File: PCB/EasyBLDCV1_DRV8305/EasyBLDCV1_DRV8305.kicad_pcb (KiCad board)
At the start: 4 copper layers, 71 parts, among them J1 10159560-A00221RLF, J2 TC2050-IDC, Q1 CSD16556Q5B, Q2 CSD16556Q5B, Q3 CSD16556Q5B, Q4 CSD16556Q5B, Q5 CSD16556Q5B, Q6 CSD16556Q5B, U1 DRV83053PHP, U2 TMS320F28027FPTT, U3 TPD4E05U06DQAR, U4 LMR16006XDDCR

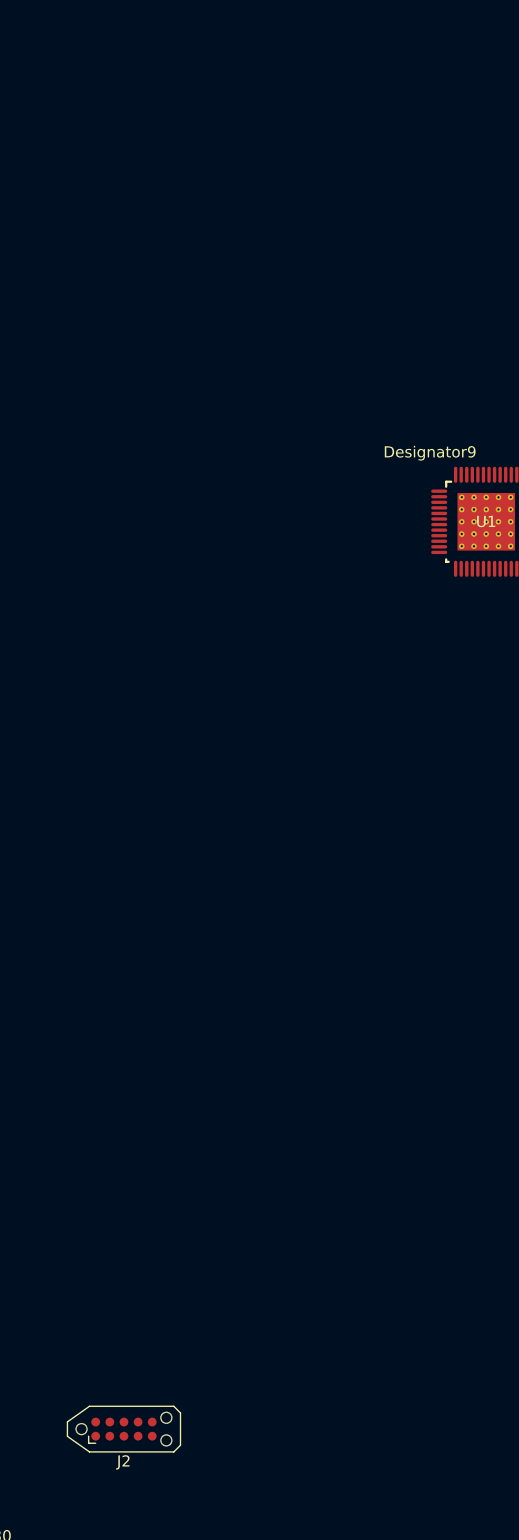
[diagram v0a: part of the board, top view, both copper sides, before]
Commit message: Updated Schematic With Missing Footprints
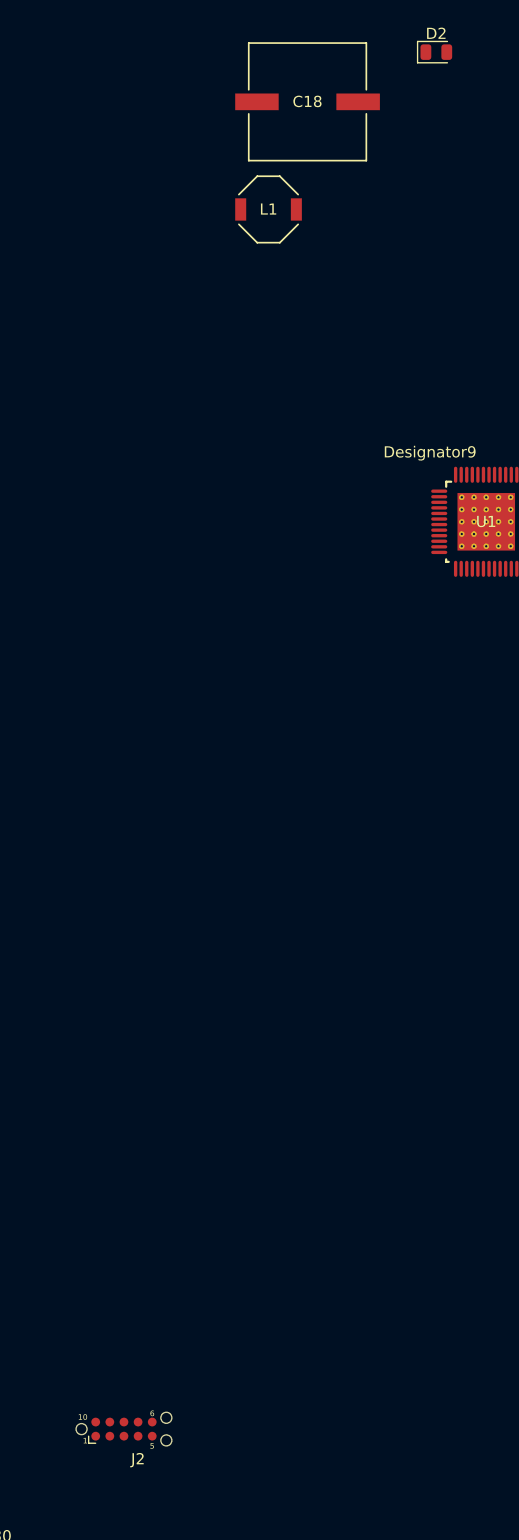
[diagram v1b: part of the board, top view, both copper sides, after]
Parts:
- added C18: 390u, EasyBLDC:CAP_FP_10P3X10P3_PAN, F.Cu at (143.5, 40.4)
- added D2: GREEN, LED_SMD:LED_0805_2012Metric, F.Cu at (155.1, 35.9)
- added L1: SD53-120-R, EasyBLDC:SD53, F.Cu at (140.0, 50.0)
- J1: footprint Connectors:AMPHENOL_10159560-A00221RLF -> EasyBLDC:AMPHENOL_10159560-A00221RLF
- J2: footprint Connector:Tag-Connect_TC2050-IDC-NL_2x05_P1.27mm_Vertical -> EasyBLDC:Tag-Connect_TC2050-IDC-NL_2x05_P1.27mm_Vertical
- Q1, Q2, Q3, Q4, Q5, Q6: footprint CSD16556Q5B:DNK0008A -> EasyBLDC:DNK0008A
- U1: footprint DRV8305:PHP0048G_N -> EasyBLDC:PHP0048G_N
- U2: footprint TMS320F28027FPTT:PT0048A_N -> EasyBLDC:PT0048A_N
- U3: footprint TPD4E05U06DQAR:DQA0010A -> EasyBLDC:DQA0010A
- U4: footprint LMR16006XDDCR:DDC0006A -> EasyBLDC:DDC0006A

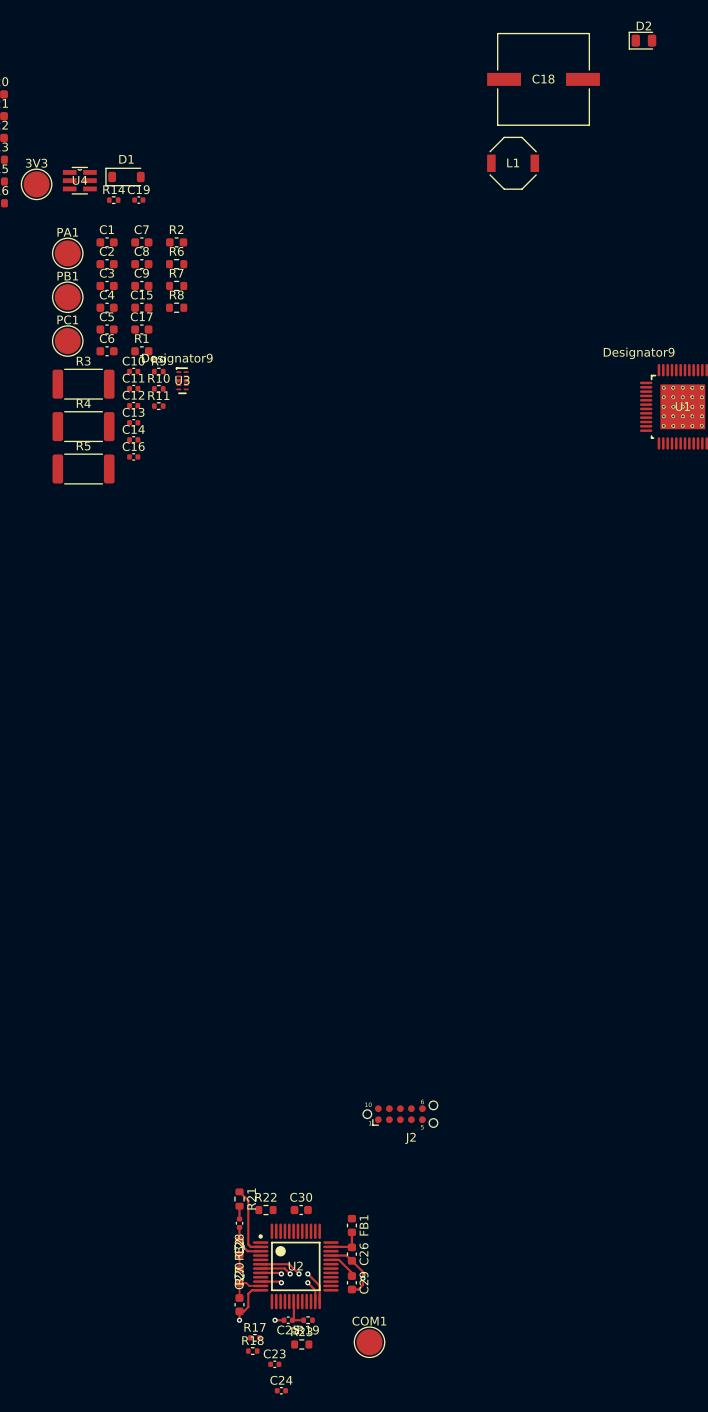
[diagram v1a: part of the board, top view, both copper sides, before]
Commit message: Progress on MCU Breakout
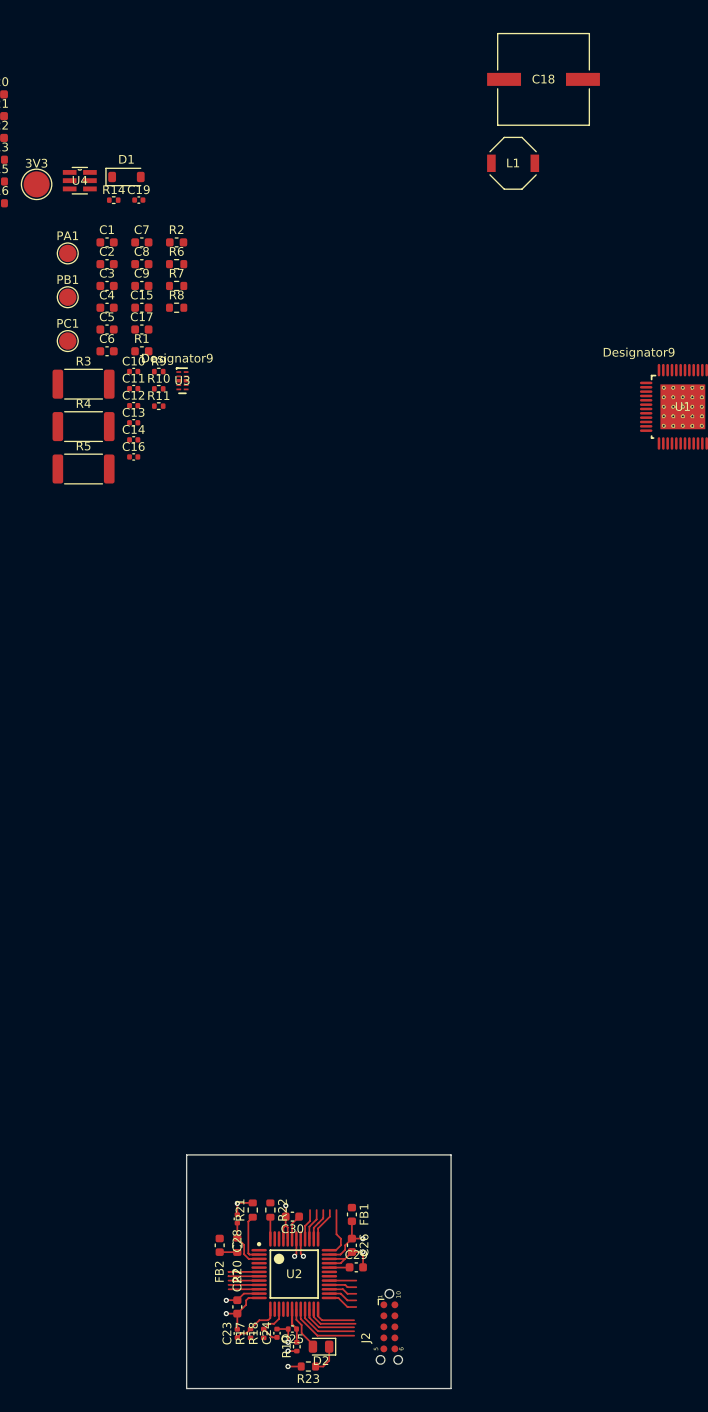
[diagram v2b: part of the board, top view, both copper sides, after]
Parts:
- removed COM1: TestPoint, TestPoint:TestPoint_Pad_D3.0mm
- PA1, PB1, PC1: footprint TestPoint:TestPoint_Pad_D3.0mm -> TestPoint:TestPoint_Pad_D2.0mm
- moved D2 155.1 mm to (117.9, 186.4), turned to 180 degrees
- moved J2 24.5 mm to (125.7, 184.2), turned to -90 degrees
- moved C24 6.65 mm to (112.8, 184.9), turned to 90 degrees
- moved C23 5.59 mm to (108.2, 184.9), turned to 90 degrees
- moved FB2 4.23 mm to (106.2, 174.8), turned to 90 degrees
- moved R19 3.31 mm to (115.1, 186.4), turned to 90 degrees
- moved R23 2.65 mm to (116.4, 188.7), turned to 180 degrees
- moved R18 2.40 mm to (111.3, 184.9), turned to 90 degrees
- moved R21 1.98 mm to (110.0, 170.7), turned to 90 degrees
- moved C29 1.85 mm to (121.9, 177.3), turned to 0 degrees
- moved FB1 1.27 mm to (121.4, 171.2)
- moved C30 1.27 mm to (114.6, 171.4), turned to 180 degrees
- moved C25 1.12 mm to (114.6, 184.4)
- moved C26 1.02 mm to (121.4, 174.8)
- moved U2 0.90 mm to (114.8, 178.1)
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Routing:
- net GND: track 15.3 -> 27.7 mm, vias 3 -> 6
- net TDI: track 0.00 -> 8.07 mm
- net TMS: track 0.00 -> 7.31 mm
- net TDO: track 0.00 -> 6.58 mm
- net nSCS: track 0.00 -> 5.84 mm
- net MCU_ISEN_A: track 0.00 -> 5.76 mm
- net MCU_ISEN_B: track 0.00 -> 5.28 mm
- net LED: track 0.00 -> 5.11 mm
- net INH_B: track 0.00 -> 3.89 mm
- net INL_B: track 0.00 -> 3.78 mm
- net INH_C: track 0.00 -> 3.68 mm
- net INL_C: track 0.00 -> 3.57 mm
- net COM: track 0.00 -> 3.54 mm
- net unconnected-(U2-ADCINA2_COMP1A_AIO2-Pad9): track 0.00 -> 3.52 mm
- net TCK: track 2.52 -> 6.04 mm, vias 1 -> 0
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- added copper zone on In1.Cu, net GND
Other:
- board outline added: 30.5 x 26.9 mm

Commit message: Continued work on layout
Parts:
- moved U1 212.7 mm to (-29.9, 174.8)
- moved C1 175.8 mm to (-31.5, 183.1), turned to 90 degrees
- moved R1 171.8 mm to (-33.5, 183.1), turned to 90 degrees
- moved R2 169.2 mm to (-32.8, 162.6), turned to 180 degrees
- moved C8 165.7 mm to (-32.3, 165.1)
- moved C7 165.4 mm to (-26.9, 168.4), turned to 180 degrees
- moved C2 163.9 mm to (-31.0, 168.7)
- moved C3 163.7 mm to (-35.6, 165.4)
- moved C9 163.7 mm to (-30.2, 166.9), turned to 180 degrees
- moved C13 160.5 mm to (-26.7, 183.1), turned to -90 degrees
- moved C14 160.4 mm to (-28.2, 183.1), turned to -90 degrees
- moved C16 160.4 mm to (-29.7, 183.1), turned to -90 degrees
- moved C15 159.2 mm to (-28.7, 164.1)
- moved C17 157.0 mm to (-22.6, 170.7)
- moved R6 145.2 mm to (227.6, 133.1)
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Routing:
- net 3.3V: track 2.05 -> 29.2 mm
- net GND: track 27.7 -> 40.1 mm, vias 6 -> 12
- net Net-(D1-K): track 0.00 -> 7.53 mm
- net PVDD: track 0.00 -> 5.87 mm, vias 0 -> 22
- net Net-(U4-FB): track 0.00 -> 5.25 mm
- net Net-(U4-CB): track 0.00 -> 2.15 mm
- added copper zone on F.Cu, net MOT_A
- added copper zone on F.Cu, net PVDD
- added copper zone on F.Cu, net SL_A
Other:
- board size 30.5 x 26.9 mm -> 42.7 x 44.7 mm

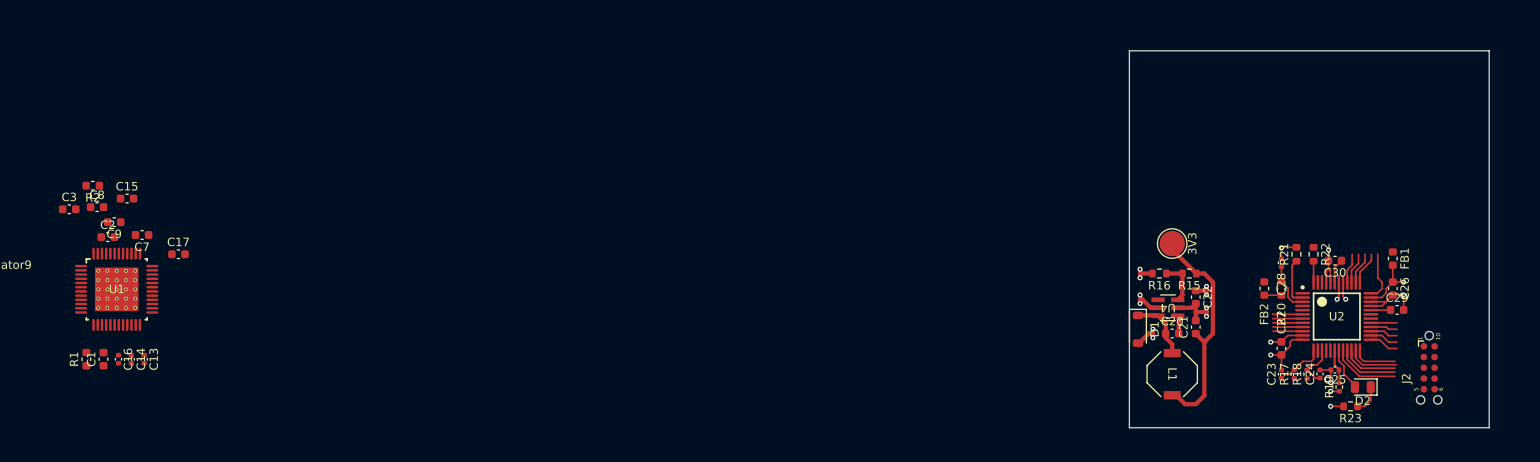
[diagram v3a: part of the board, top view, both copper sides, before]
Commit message: Started DRV Breakout
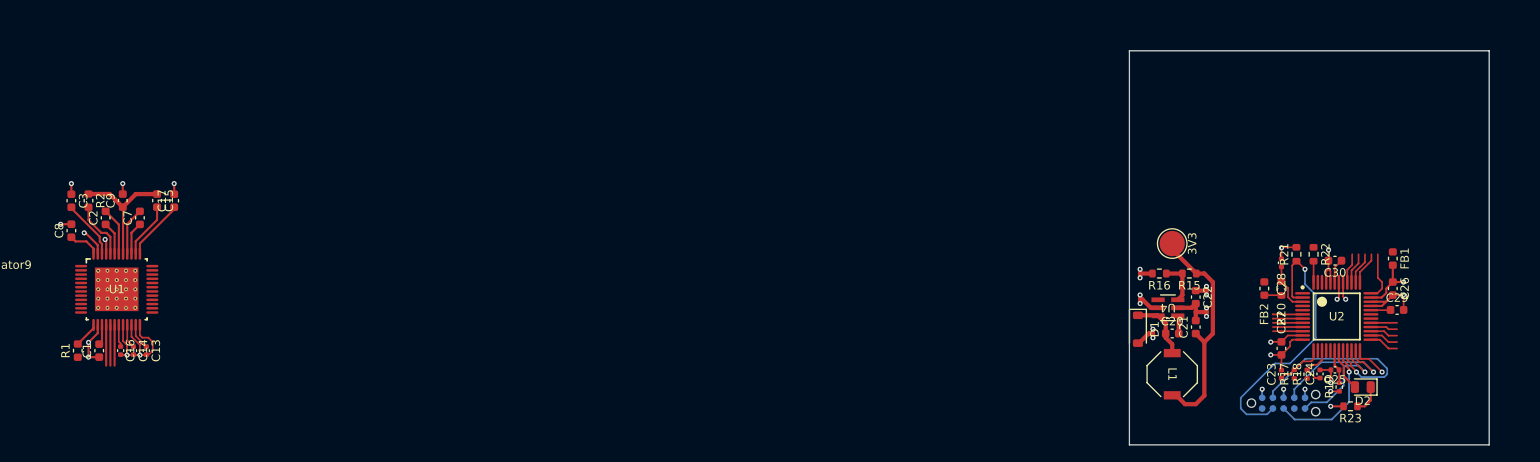
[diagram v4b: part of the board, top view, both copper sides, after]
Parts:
- J2: moved to B.Cu
- moved J2 17.8 mm to (108.5, 188.3), turned to 0 degrees
- moved C17 6.37 mm to (-23.1, 164.3), turned to 90 degrees
- moved C8 4.13 mm to (-35.3, 167.9), turned to 90 degrees
- moved C15 3.56 mm to (-25.1, 164.3), turned to -90 degrees
- moved C9 2.75 mm to (-29.2, 164.3), turned to 90 degrees
- moved C2 2.30 mm to (-31.2, 166.4), turned to 90 degrees
- moved C7 2.05 mm to (-27.2, 166.4), turned to 90 degrees
- moved R2 1.84 mm to (-33.3, 164.3), turned to -90 degrees
- moved R1 1.44 mm to (-34.5, 182.1)
- moved C1 1.14 mm to (-32.0, 182.1)
- moved C16 1.05 mm to (-29.5, 182.1)
- moved C14 1.05 mm to (-27.9, 182.1)
- moved C3 1.05 mm to (-35.3, 164.3), turned to -90 degrees
- moved C13 1.05 mm to (-26.4, 182.1)
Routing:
- net GND: track 40.1 -> 70.4 mm, vias 12 -> 23
- net nTRST: track 5.68 -> 33.2 mm, vias 0 -> 1
- net TMS: track 7.31 -> 24.1 mm, vias 0 -> 1
- net PVDD: track 5.87 -> 20.8 mm
- net TCK: track 6.04 -> 15.9 mm, vias 0 -> 1
- net TDI: track 8.07 -> 15.6 mm, vias 0 -> 1
- net TDO: track 6.58 -> 14.0 mm, vias 0 -> 1
- net Net-(U1-VCP_LSD): track 0.00 -> 7.19 mm
- net Net-(U1-DVDD): track 0.00 -> 7.01 mm
- net Net-(U1-VDRAIN): track 0.00 -> 6.93 mm
- net Net-(U1-VCPH): track 0.00 -> 6.57 mm
- net Net-(U1-CP1L): track 0.00 -> 5.67 mm
- net Net-(U1-CP2L): track 0.00 -> 5.65 mm
- net ISEN_C: track 1.02 -> 5.84 mm
- net ISEN_B: track 0.00 -> 4.83 mm
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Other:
- board size 42.7 x 44.7 mm -> 42.7 x 46.7 mm

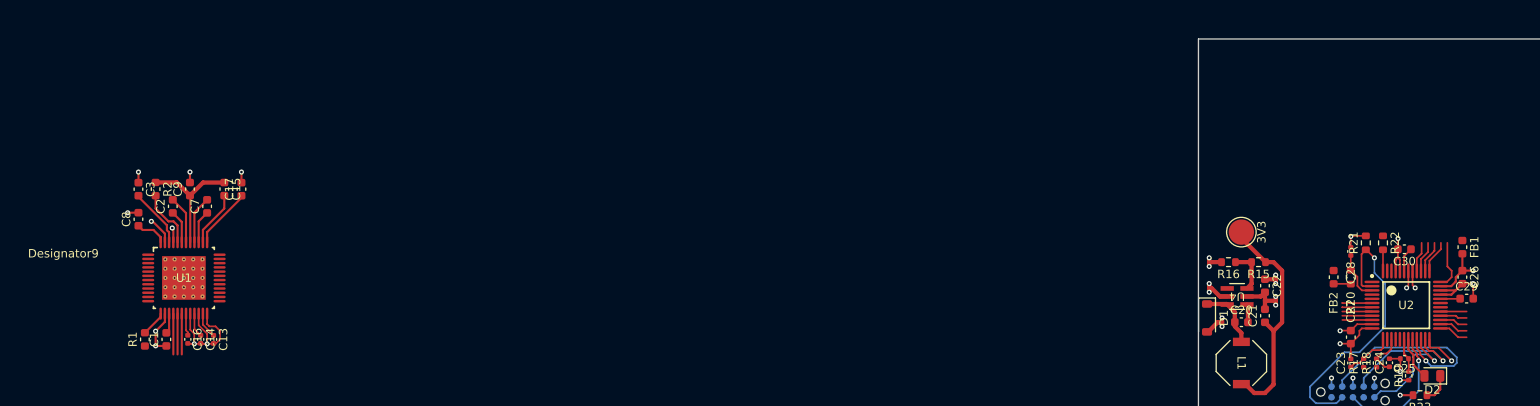
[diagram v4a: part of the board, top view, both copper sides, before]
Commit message: Continued work on drv8305 breakout
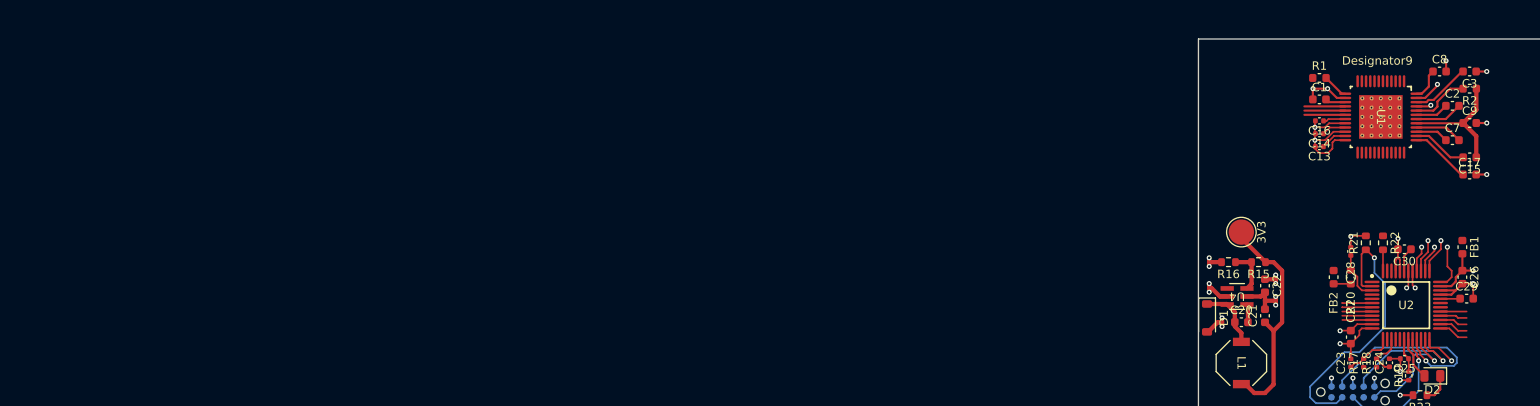
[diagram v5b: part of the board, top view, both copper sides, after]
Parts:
- moved C3 158.2 mm to (122.3, 150.4), turned to 180 degrees
- moved R2 156.0 mm to (122.3, 152.4), turned to 180 degrees
- moved C8 155.0 mm to (118.7, 150.4), turned to 0 degrees
- moved C2 151.9 mm to (120.2, 154.5), turned to 0 degrees
- moved C9 151.7 mm to (122.3, 156.5), turned to 0 degrees
- moved C7 147.6 mm to (120.2, 158.5), turned to 0 degrees
- moved C15 147.5 mm to (122.3, 160.6), turned to 180 degrees
- moved C17 145.4 mm to (122.3, 162.6), turned to 0 degrees
- moved U1 143.0 mm to (111.8, 155.8), turned to -90 degrees
- moved R1 142.4 mm to (104.5, 151.2), turned to 0 degrees
- moved C1 139.4 mm to (104.5, 153.7), turned to 0 degrees
- moved C16 136.4 mm to (104.5, 156.2), turned to 180 degrees
- moved C14 134.7 mm to (104.5, 157.8), turned to 180 degrees
- moved C13 132.9 mm to (104.5, 159.3), turned to 180 degrees
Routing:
- net nSCS: track 5.84 -> 5.33 mm, vias 0 -> 1
- net INL_C: track 3.57 -> 3.06 mm, vias 0 -> 1
- net INL_B: track 3.78 -> 3.28 mm, vias 0 -> 1
- net INH_C: track 3.68 -> 3.93 mm, vias 0 -> 1
- net INH_B: track 3.89 -> 4.15 mm, vias 0 -> 1

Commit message: Initial Layout For Mosfets
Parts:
- moved C18 122.9 mm to (86.6, 149.4)
- moved R8 77.1 mm to (213.0, 164.3)
- moved Q4 73.8 mm to (229.4, 148.6)
- moved Q6 72.9 mm to (229.3, 160.8)
- moved Q3 72.5 mm to (226.1, 142.0)
- moved C12 72.0 mm to (210.4, 171.0)
- moved C6 72.0 mm to (207.3, 164.7)
- moved R11 72.0 mm to (213.3, 171.1)
- moved Q5 71.5 mm to (226.1, 154.2)
- moved R7 65.8 mm to (211.0, 148.6), turned to 180 degrees
- moved PC1 58.8 mm to (231.5, 154.9)
- moved R10 52.7 mm to (211.5, 146.8)
- moved PB1 51.6 mm to (231.5, 142.7)
- moved C5 50.2 mm to (218.5, 143.0), turned to -90 degrees
- moved C11 50.0 mm to (211.5, 145.3)
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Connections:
- Q1 pad 9: (no net) -> PVDD
- Q2 pad 9: (no net) -> MOT_A
- Q3 pad 9: (no net) -> PVDD
- Q4 pad 9: (no net) -> MOT_B
- Q5 pad 9: (no net) -> PVDD
- Q6 pad 9: (no net) -> MOT_C
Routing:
- net GND: track 70.4 -> 75.2 mm, vias 23 -> 155
- net PVDD: track 20.8 -> 25.6 mm, vias 22 -> 76
- net VSEN_B: track 3.53 -> 7.16 mm
- net VSEN_A: track 3.53 -> 5.65 mm
- net GH_A: track 0.00 -> 1.27 mm, vias 0 -> 1
- net GH_B: track 0.00 -> 1.18 mm, vias 0 -> 1
- net GH_C: track 0.00 -> 1.12 mm, vias 0 -> 1
- added copper zone on F.Cu, net GND
- added copper zone on F.Cu, net MOT_B
- added copper zone on F.Cu, net MOT_C
- added copper zone on F.Cu, net SL_B
- added copper zone on F.Cu, net SL_C
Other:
- board size 42.7 x 46.7 mm -> 46.9 x 46.7 mm
